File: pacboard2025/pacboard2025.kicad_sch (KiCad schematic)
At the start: 10 parts, among them M1 Motor Placeholder, U1 VL53L4CXV0DH/1, U10 ProS3, U12 TPS3847085DBVR, U2 BNO085, U6 DRV8876, U7 D24V50F5, U9 J107F1CS1224VDC.36

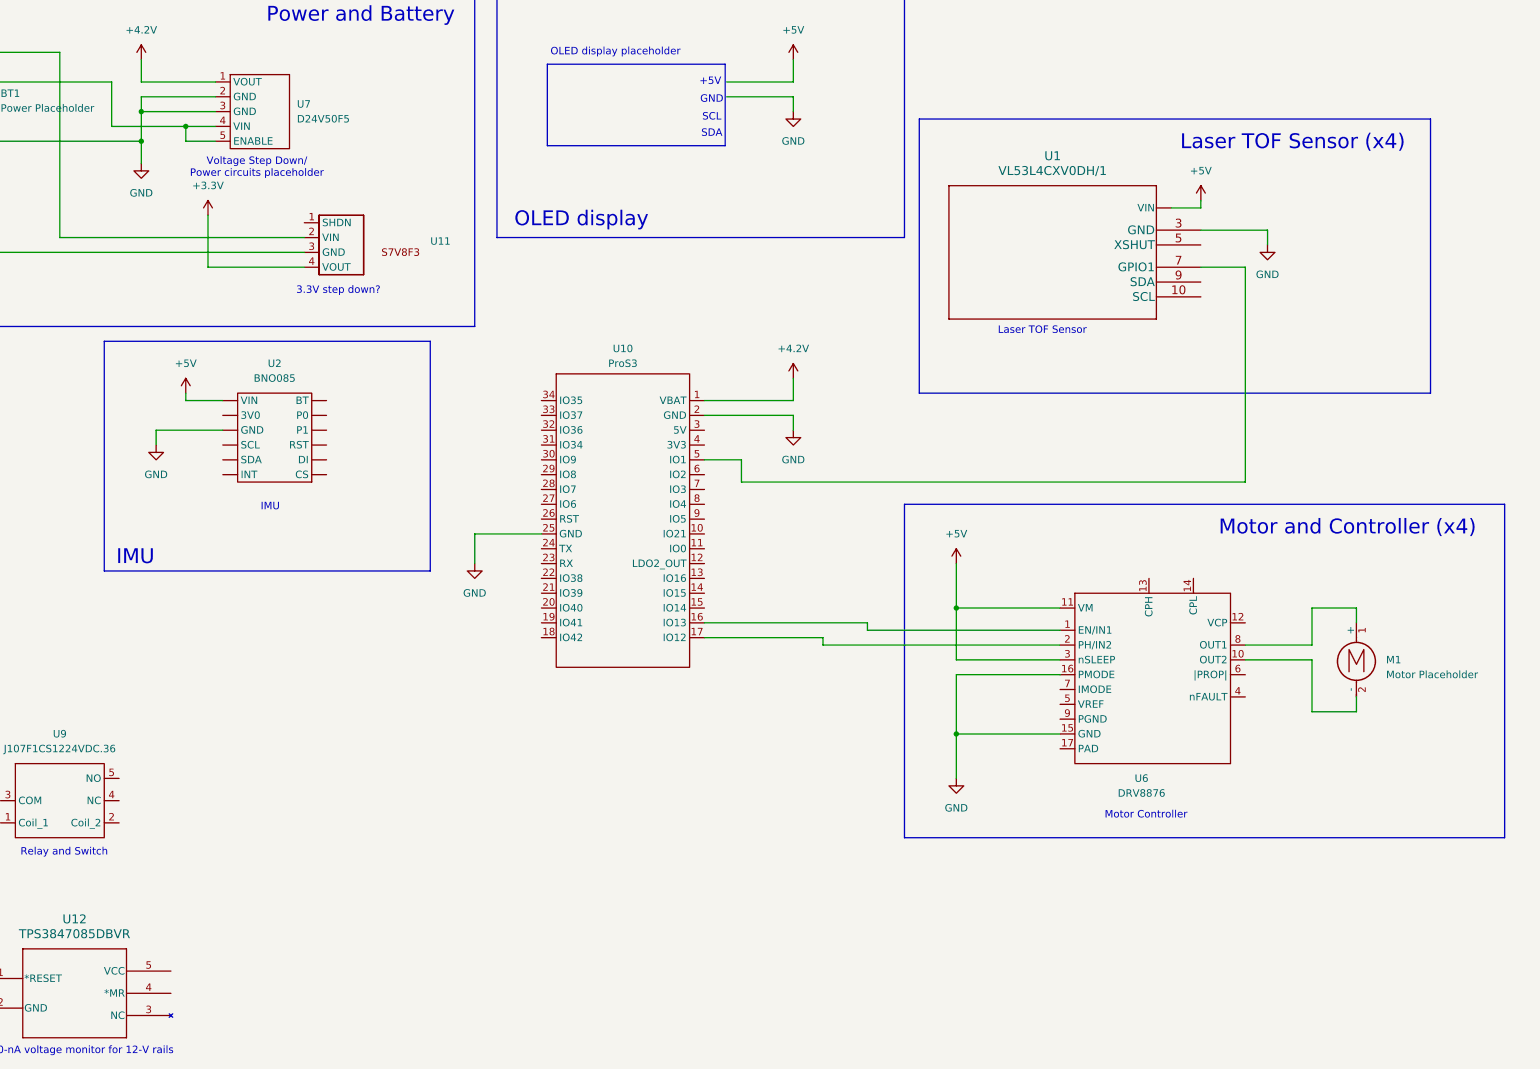
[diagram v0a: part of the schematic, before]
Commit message: Changed motor controller schematic
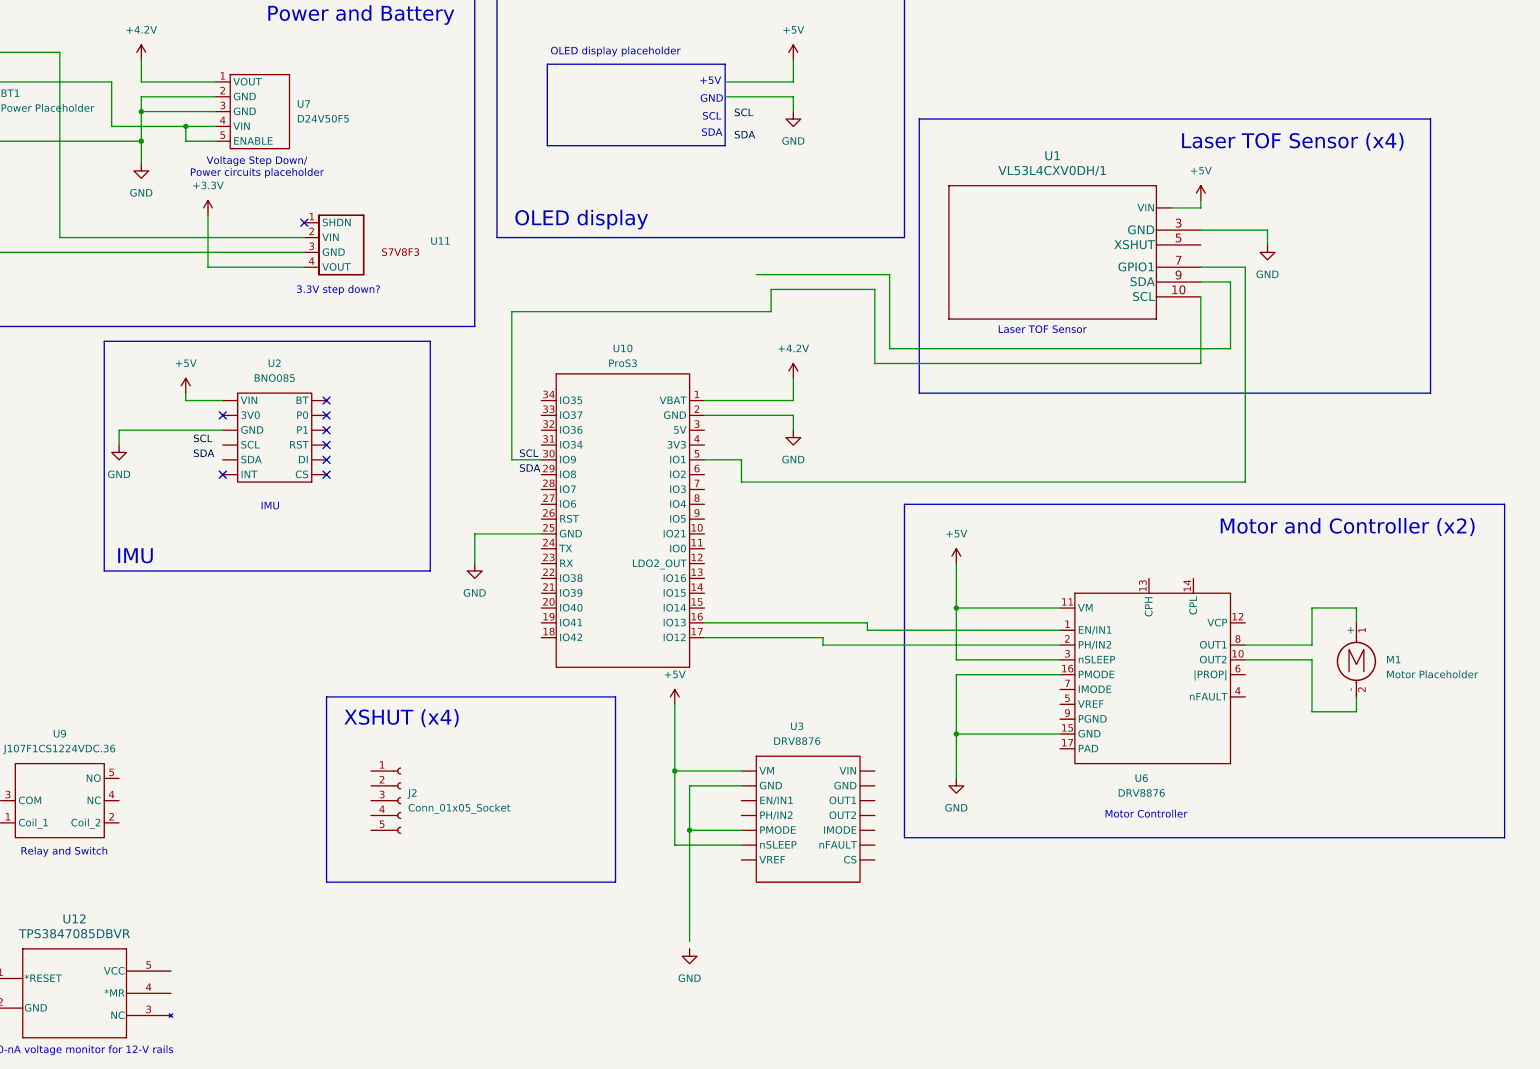
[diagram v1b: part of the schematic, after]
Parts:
- added J2: Conn_01x05_Socket, symbol Connector:Conn_01x05_Socket
- added U3: DRV8876, symbol Pacbots2023:DRV8876
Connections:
- net +5V: now also U3. (nSLEEP)
- net SCL: now reaches U10.30 (IO9)
- net SCL: now also U1.10 (SCL)
- no-connect marks 0 -> 9
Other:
- note added: "Motor and Controller (x2)"
- note added: "XSHUT (x4)"
- note removed: "Motor and Controller (x4)"

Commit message: PCB design
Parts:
- removed BT1: Power Placeholder, symbol Device:Battery_Cell
- removed J2: Conn_01x05_Socket, symbol Connector:Conn_01x05_Socket
- removed M1: Motor Placeholder, symbol Motor:Motor_DC
- removed U1: VL53L4CXV0DH/1, LGA12_STM, symbol PacbotsParts:VL53L4CXV0DH/1
- removed U10: ProS3, symbol PacbotsParts:ProS3
- removed U11: ~, symbol PacbotsParts:S7V8F3
- removed U12: TPS3847085DBVR, DBV5_TEX, symbol PacbotsParts:TPS3847085DBVR
- removed U2: BNO085, symbol PacbotsParts:BNO085
- removed U3: DRV8876, symbol Pacbots2023:DRV8876
- removed U6: DRV8876, symbol PacbotsParts:DRV8876
- removed U7: D24V50F5, symbol PacbotsParts:D24V50F5
- removed U9: J107F1CS1224VDC.36, symbol PacbotsParts:J107F1CS1224VDC.36
- added C1, C2, C3, C4: 0.1uF, Capacitor_SMD:C_0805_2012Metric_Pad1.18x1.45mm_HandSolder, symbol Device:C_Small
- added C5, C6: 0.1uF, Capacitor_SMD:C_0805_2012Metric_Pad1.18x1.45mm_HandSolder, symbol Device:C
- added Conn_01x04_Socket1: TOF_STEMMA, board1_footprints:Stemma QT, symbol Connector:Conn_01x04_Socket
- added Conn_01x06_Socket2: TOF_INTR_CONN, Connector_PinHeader_2.54mm:PinHeader_1x06_P2.54mm_Vertical, symbol Connector:Conn_01x06_Socket
- added D1: D, Capacitor_SMD:C_0805_2012Metric_Pad1.18x1.45mm_HandSolder, symbol Device:D
- added J1: XT30 Male Connector, Connector_AMASS:AMASS_XT30U-M_1x02_P5.0mm_Vertical, symbol Connector_Generic:Conn_01x02
- added J107F1: ~, board1_footprints:J107, symbol board1_libs:J107F
- added LED1, LED2, LED3, LED4: Neopixel, board1_footprints:Neopixel, symbol board1_libs:Neopixel
- added LP3470A1: ~, Package_TO_SOT_SMD:SOT-23-5, symbol Bat_lib:LP3470A
- added MC1, MC2: DRV8876, board1_footprints:DRV8876, symbol board1_libs:DRV8876
- added MOTOR1, MOTOR2: Conn_01x06_Pin, board1_footprints:ZH1.5-6, symbol Connector:Conn_01x06_Pin
- added R1: 4.7k, Resistor_SMD:R_0805_2012Metric_Pad1.20x1.40mm_HandSolder, symbol Device:R
- added R2: 500, Resistor_SMD:R_0805_2012Metric_Pad1.20x1.40mm_HandSolder, symbol Device:R
- added R3: 150k, Resistor_SMD:R_0805_2012Metric_Pad1.20x1.40mm_HandSolder, symbol Device:R_US
- added R4: 100k, Resistor_SMD:R_0805_2012Metric_Pad1.20x1.40mm_HandSolder, symbol Device:R_US
- added U2: D24V50F5, Connector_PinHeader_2.54mm:PinHeader_1x05_P2.54mm_Vertical, symbol board1_libs:D24V50F5
- added U3: ProS3, board1_footprints:ProS3_TH (1), symbol board1_libs:ProS3
- added U6: BNO085, board1_footprints:BNU0085, symbol board1_libs:BNO085
- added XSHUT_CONN1: Conn_01x06_Socket, Connector_PinHeader_2.54mm:PinHeader_1x06_P2.54mm_Vertical, symbol Connector:Conn_01x06_Socket
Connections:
- net +3.3V: now also Conn_01x04_Socket1.2 (Pin_2), MC1.6 (nSLEEP), MC2.6 (nSLEEP), MOTOR1.5 (Pin_5), MOTOR2.5 (Pin_5), R1.1, U3.12 (LDO2_OUT), U3.4 (3V3), U6.4 (P1), U6.7 (VIN)
- net GND: now also C1.2, C2.2, C3.2, C4.2, Conn_01x04_Socket1.1 (Pin_1), J1.1 (Pin_1), LED1.2 (GND), LED2.2 (GND), LED3.2 (GND), LED4.2 (GND), MC1.13 (GND), MC1.2 (GND), MC1.5 (PMODE), MC2.13 (GND), MC2.2 (GND), MC2.5 (PMODE), MOTOR1.2 (Pin_2), MOTOR2.2 (Pin_2), R1.2, U2.2 (GND), U2.3 (GND), U3.2 (GND), U3.25 (GND), U6.9 (GND)
- new net: LED1.3 (DIN), R2.2
- new net: LP3470A1.4 (VCC), R3.2, R4.1
- new net: D1.2 (A), J107F1.2 (Coil_1), LP3470A1.5 (RESET)
- new net: C6.1, LP3470A1.2 (GND)
- new net: LED3.1 (DOUT), LED4.3 (DIN)
- new net: LED2.1 (DOUT), LED3.3 (DIN)
- new net: LED1.1 (DOUT), LED2.3 (DIN)
- new net +12V: MC1.14 (VIN), MC2.14 (VIN)
- new net 12V: J107F1.1 (COM), U2.4 (VIN)
- new net 1_ENCA: MOTOR1.3 (Pin_3), U3.13 (IO16)
- new net 1_ENCB: MOTOR1.4 (Pin_4), U3.14 (IO15)
- new net 1_PWM1: MC1.3 (EN/IN1), U3.34 (IO35)
- new net 1_PWM2: MC1.4 (PH/IN2), U3.33 (IO37)
- new net 2_ENCA: MOTOR2.3 (Pin_3), U3.15 (IO14)
- new net 2_ENCB: MOTOR2.4 (Pin_4), U3.16 (IO13)
- new net 2_PWM1: MC2.3 (EN/IN1), U3.32 (IO36)
- new net 2_PWM2: MC2.4 (PH/IN2), U3.31 (IO34)
- new net 5V: C1.1, C2.1, C3.1, C4.1, LED1.4 (VDD), LED2.4 (VDD), LED3.4 (VDD), LED4.4 (VDD), U2.1 (VOUT), U3.3 (5V)
- new net BAT_12V: C5.2, D1.1 (K), J1.2 (Pin_2), J107F1.3 (Coil_2), J107F1.5 (NC), R3.1
- new net GNDREF: C5.1, C6.2, R4.2
- new net IMU_INTR: U3.27 (IO6), U6.12 (INT)
- new net INTR_TOF1: Conn_01x06_Socket2.6 (Pin_6), U3.5 (IO1)
- new net INTR_TOF2: Conn_01x06_Socket2.5 (Pin_5), U3.6 (IO2)
- new net INTR_TOF3: Conn_01x06_Socket2.4 (Pin_4), U3.7 (IO3)
- new net INTR_TOF4: Conn_01x06_Socket2.3 (Pin_3), U3.8 (IO4)
- new net INTR_TOF5: Conn_01x06_Socket2.2 (Pin_2), U3.9 (IO5)
- new net INTR_TOF6: Conn_01x06_Socket2.1 (Pin_1), U3.10 (IO21)
- new net LED_DATA: R2.1, U3.28 (IO7)
- new net MOTOR1_V+: MC1.12 (OUT1), MOTOR1.1 (Pin_1)
- new net MOTOR1_V-: MC1.11 (OUT2), MOTOR1.6 (Pin_6)
- new net MOTOR2_V+: MC2.12 (OUT1), MOTOR2.1 (Pin_1)
- new net MOTOR2_V-: MC2.11 (OUT2), MOTOR2.6 (Pin_6)
- new net SERIAL_CLOCK_LINE: Conn_01x04_Socket1.4 (Pin_4), U3.30 (IO9)
- new net SERIAL_DATA_LINE: Conn_01x04_Socket1.3 (Pin_3), U3.29 (IO8)
- new net UART_RX: U3.23 (RX), U6.11 (SDA)
- new net UART_TX: U3.24 (TX), U6.10 (SCL)
- new net XSHUT_TOF1: U3.22 (IO38), XSHUT_CONN1.6 (Pin_6)
- new net XSHUT_TOF2: U3.21 (IO39), XSHUT_CONN1.5 (Pin_5)
- new net XSHUT_TOF3: U3.20 (IO40), XSHUT_CONN1.4 (Pin_4)
- new net XSHUT_TOF4: U3.19 (IO41), XSHUT_CONN1.3 (Pin_3)
- new net XSHUT_TOF5: U3.18 (IO42), XSHUT_CONN1.2 (Pin_2)
- new net XSHUT_TOF6: U3.17 (IO12), XSHUT_CONN1.1 (Pin_1)
- no-connect marks 9 -> 23
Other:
- note added: "*verify orientation of zh (motor encoder) pins are correct with footprint"
- note added: "12-5V Step-Down"
- note added: "Battery Management"
- note added: "ESP32 ProS3"
- note added: "IMU Sensor"
- note added: "Motor Controllers"
- note added: "Motor Encoders"
- note added: "Neopixels LEDs"
- note added: "Notes: IMU interrupt connect to RTC5 on ProS3 Figure out inteerrupt P1 pins on board since they're not on stemma-qt"
- note added: "TOF Sensors"
- note added: "all TOFs chained together"
- note added: "intr is GPIO pin on TOF"
- note added: "pullup resistor for i2c"
- note added: "update diode footprint"
- note removed: "+5V"
- note removed: "3.3V step down?"
- note removed: "380-nA voltage monitor for 12-V rails"
- note removed: "GND"
- note removed: "IMU"
- note removed: "Laser TOF Sensor"
- note removed: "Laser TOF Sensor (x4)"
- note removed: "Motor Controller"
- note removed: "Motor and Controller (x2)"
- note removed: "OLED display"
- note removed: "OLED display placeholder"
- note removed: "Power and Battery"
- note removed: "Relay and Switch"
- note removed: "SCL"
- note removed: "SDA"
- note removed: "Voltage Step Down/ Power circuits placeholder"
- note removed: "XSHUT (x4)"

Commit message: some changes to pcb
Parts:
- Conn_01x04_Socket1: footprint board1_footprints:Stemma QT -> Connector_JST:JST_SH_SM04B-SRSS-TB_1x04-1MP_P1.00mm_Horizontal
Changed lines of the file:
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@@
 			)
 		)
-		(property "Footprint" "board1_footprints:Stemma QT"
+		(property "Footprint" "Connector_JST:JST_SH_SM04B-SRSS-TB_1x04-1MP_P1.00mm_Horizontal"
 			(at 67.31 133.35 0)
 			(effects

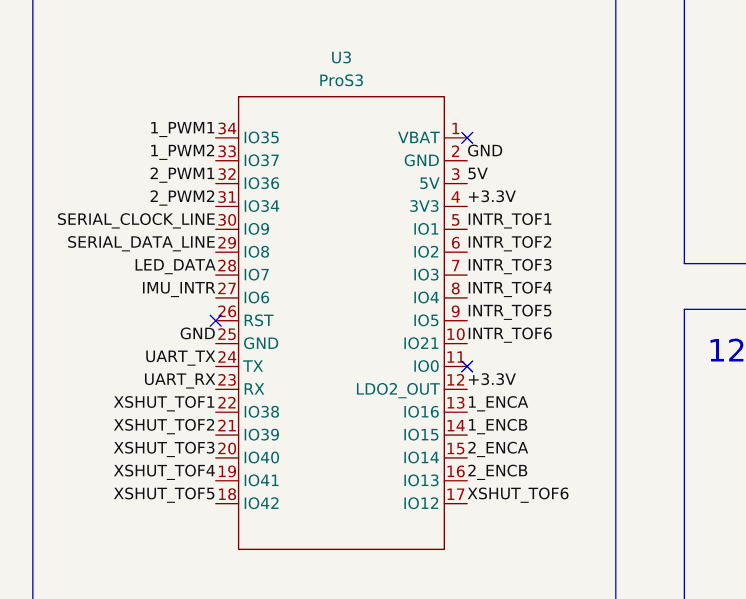
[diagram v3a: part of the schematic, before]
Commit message: Changed layout to account for battery and motors, tried routing stuff
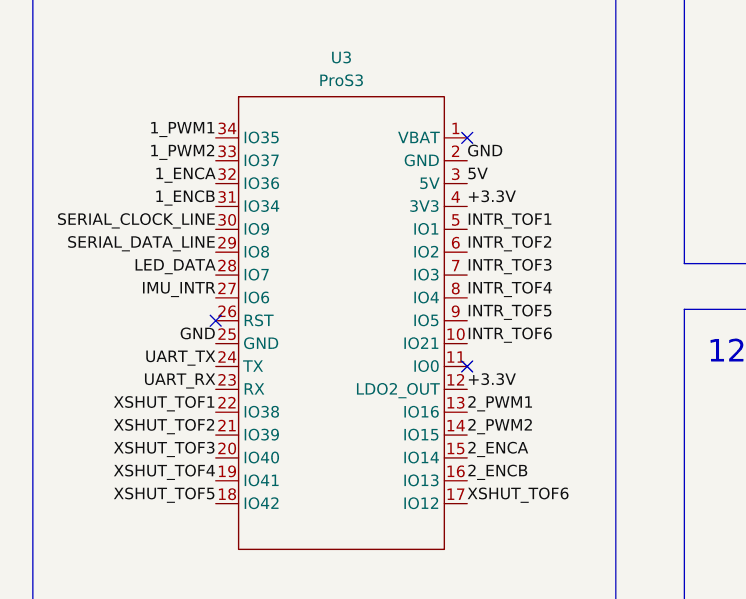
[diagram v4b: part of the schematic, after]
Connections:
- net 1_ENCA: now also U3.32 (IO36); no longer U3.13 (IO16)
- net 1_ENCB: now also U3.31 (IO34); no longer U3.14 (IO15)
- net 2_PWM1: now also U3.13 (IO16); no longer U3.32 (IO36)
- net 2_PWM2: now also U3.14 (IO15); no longer U3.31 (IO34)
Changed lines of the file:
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@@
 		)
 	)
-	(label "1_ENCA"
+	(label "2_PWM1"
 		(at 69.85 76.2 0)
 		(fields_autoplaced yes)
@@
 		)
 	)
-	(label "2_PWM1"
+	(label "1_ENCA"
 		(at 41.91 50.8 180)
 		(fields_autoplaced yes)
@@
 		)
 	)
-	(label "2_PWM2"
+	(label "1_ENCB"
 		(at 41.91 53.34 180)
 		(fields_autoplaced yes)
@@
 		)
 	)
-	(label "1_ENCB"
+	(label "2_PWM2"
 		(at 69.85 78.74 0)
 		(fields_autoplaced yes)
